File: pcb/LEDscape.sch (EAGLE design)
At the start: 31 parts, among them IC1 MAX3041CUE, IC2 MAX3041CUE, IC3 MAX3041CUE, IC4 MAX3041CUE, IC5 MAX3041CUE, IC6 MAX3041CUE, IC7 MAX3041CUE, IC8 MAX3041CUE

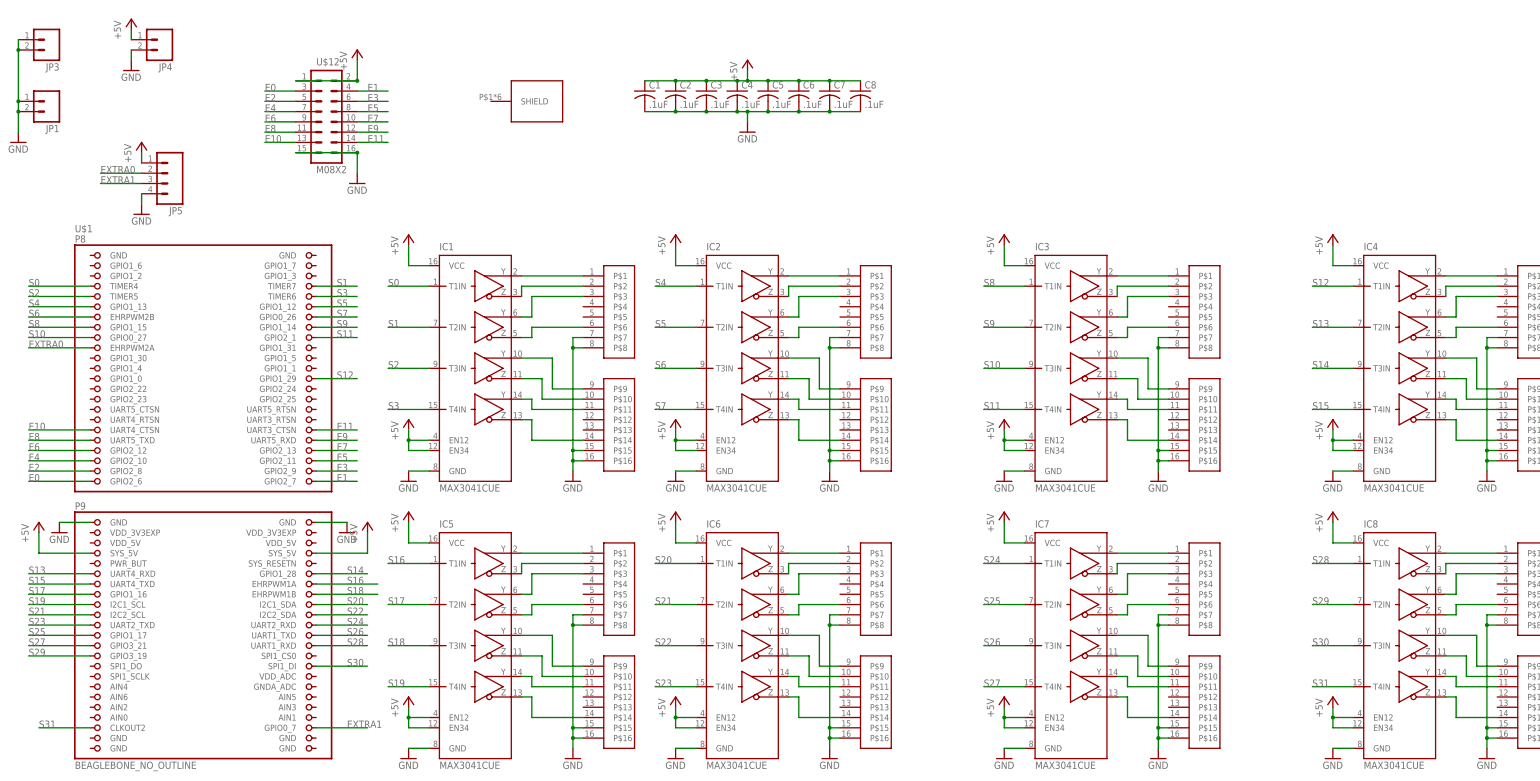
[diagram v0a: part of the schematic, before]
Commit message: RevB LEDscape board design: slightly bigger, debug headers for all signals
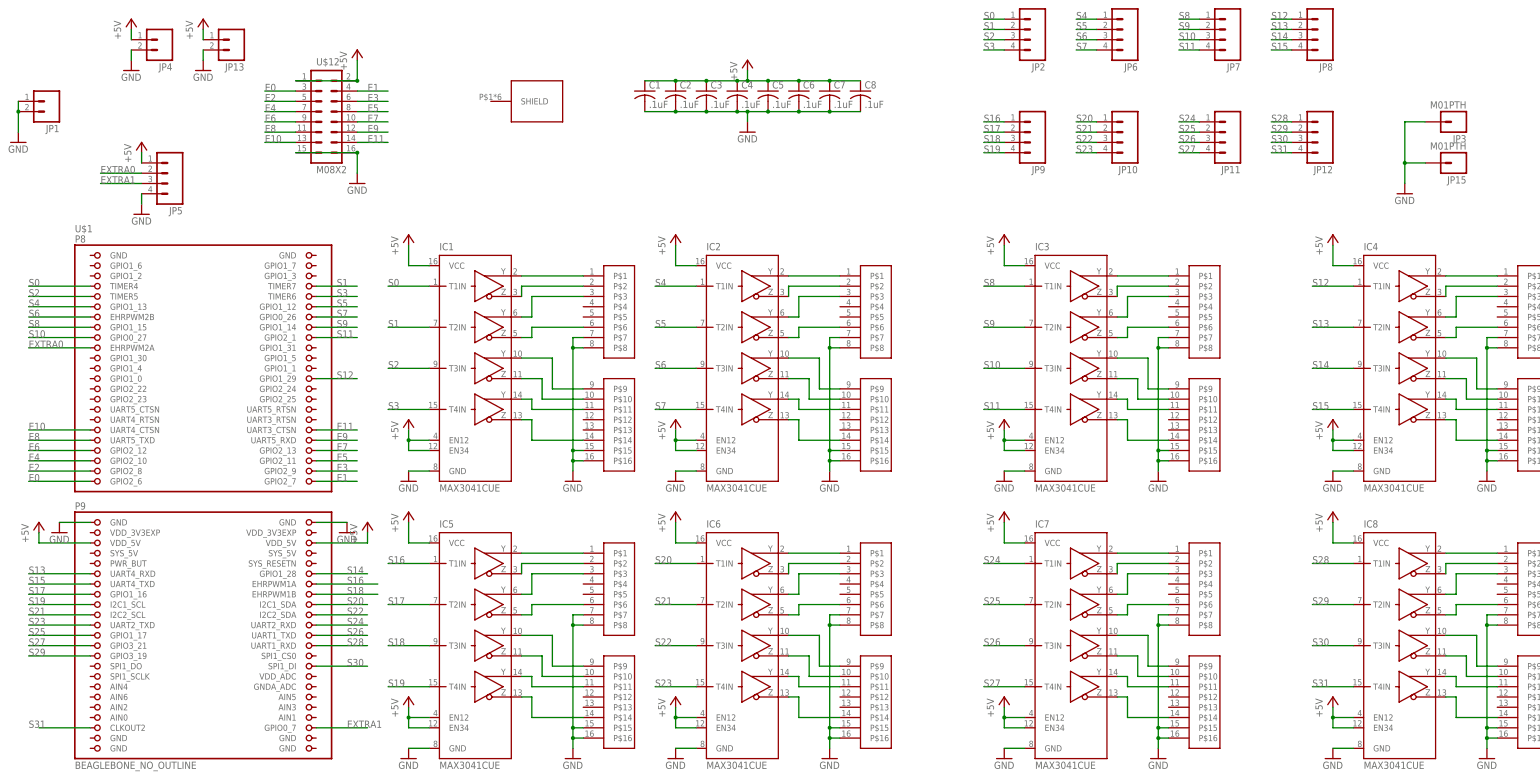
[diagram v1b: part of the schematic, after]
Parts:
- added JP10, JP11, JP12, JP2, JP6, JP7, JP8, JP9: (no value), SparkFun-Connectors:M041X04_NO_SILK
- added JP13: (no value), SparkFun-Connectors:M025MM
- added JP15: M01PTH, SparkFun-Connectors:M01PTH
- JP3: value (none) -> M01PTH; device SparkFun-Connectors:M025MM -> SparkFun-Connectors:M01PTH
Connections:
- net +5V: now also JP13.1, U$1.VDD_5V@1, U$1.VDD_5V@2; no longer U$1.SYS_5V@1, U$1.SYS_5V@2
- net GND: now also JP13.2, JP15.1; no longer JP3.2
- net S0: now also JP2.1
- net S1: now also JP2.2
- net S10: now also JP7.3
- net S11: now also JP7.4
- net S12: now also JP8.1
- net S13: now also JP8.2
- net S14: now also JP8.3
- net S15: now also JP8.4
- net S16: now also JP9.1
- net S17: now also JP9.2
- net S18: now also JP9.3
- net S19: now also JP9.4
- net S2: now also JP2.3
- net S20: now also JP10.1
- net S21: now also JP10.2
- net S22: now also JP10.3
- net S23: now also JP10.4
- net S24: now also JP11.1
- net S25: now also JP11.2
- net S26: now also JP11.3
- net S27: now also JP11.4
- net S28: now also JP12.1
- net S29: now also JP12.2
- net S3: now also JP2.4
- net S30: now also JP12.3
- net S31: now also JP12.4
- net S4: now also JP6.1
- net S5: now also JP6.2
- net S6: now also JP6.3
- net S7: now also JP6.4
- net S8: now also JP7.1
- net S9: now also JP7.2

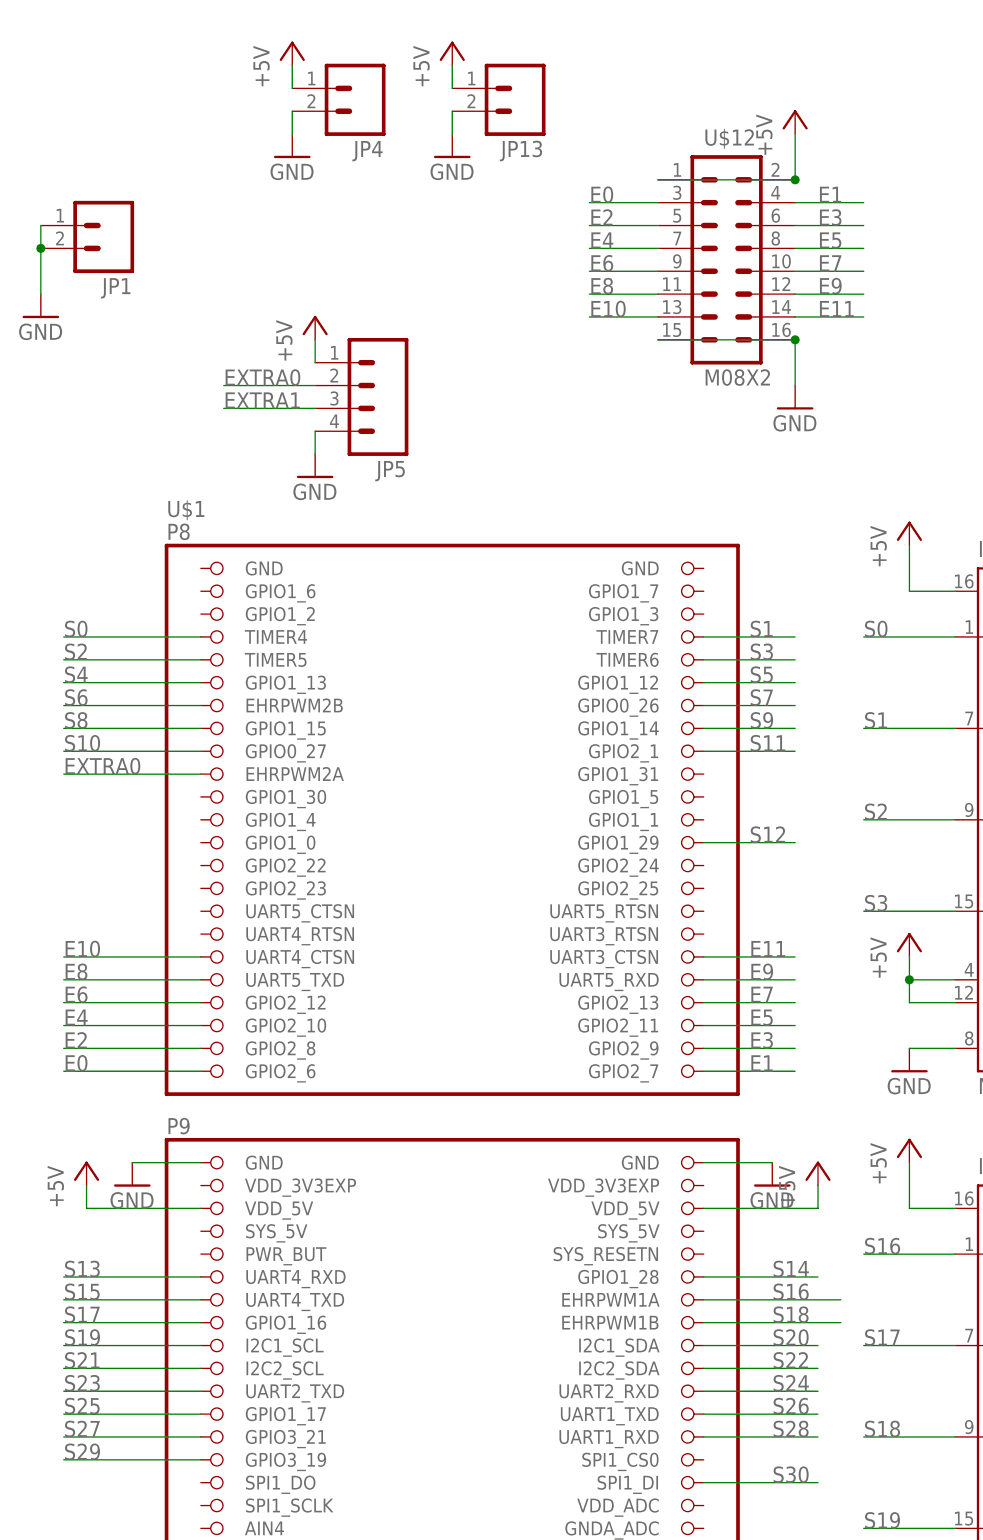
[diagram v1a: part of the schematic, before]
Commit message: Redesign transmitter PCB to use top and bottom ground planes, and one track for +5V- should be much easier to work with.
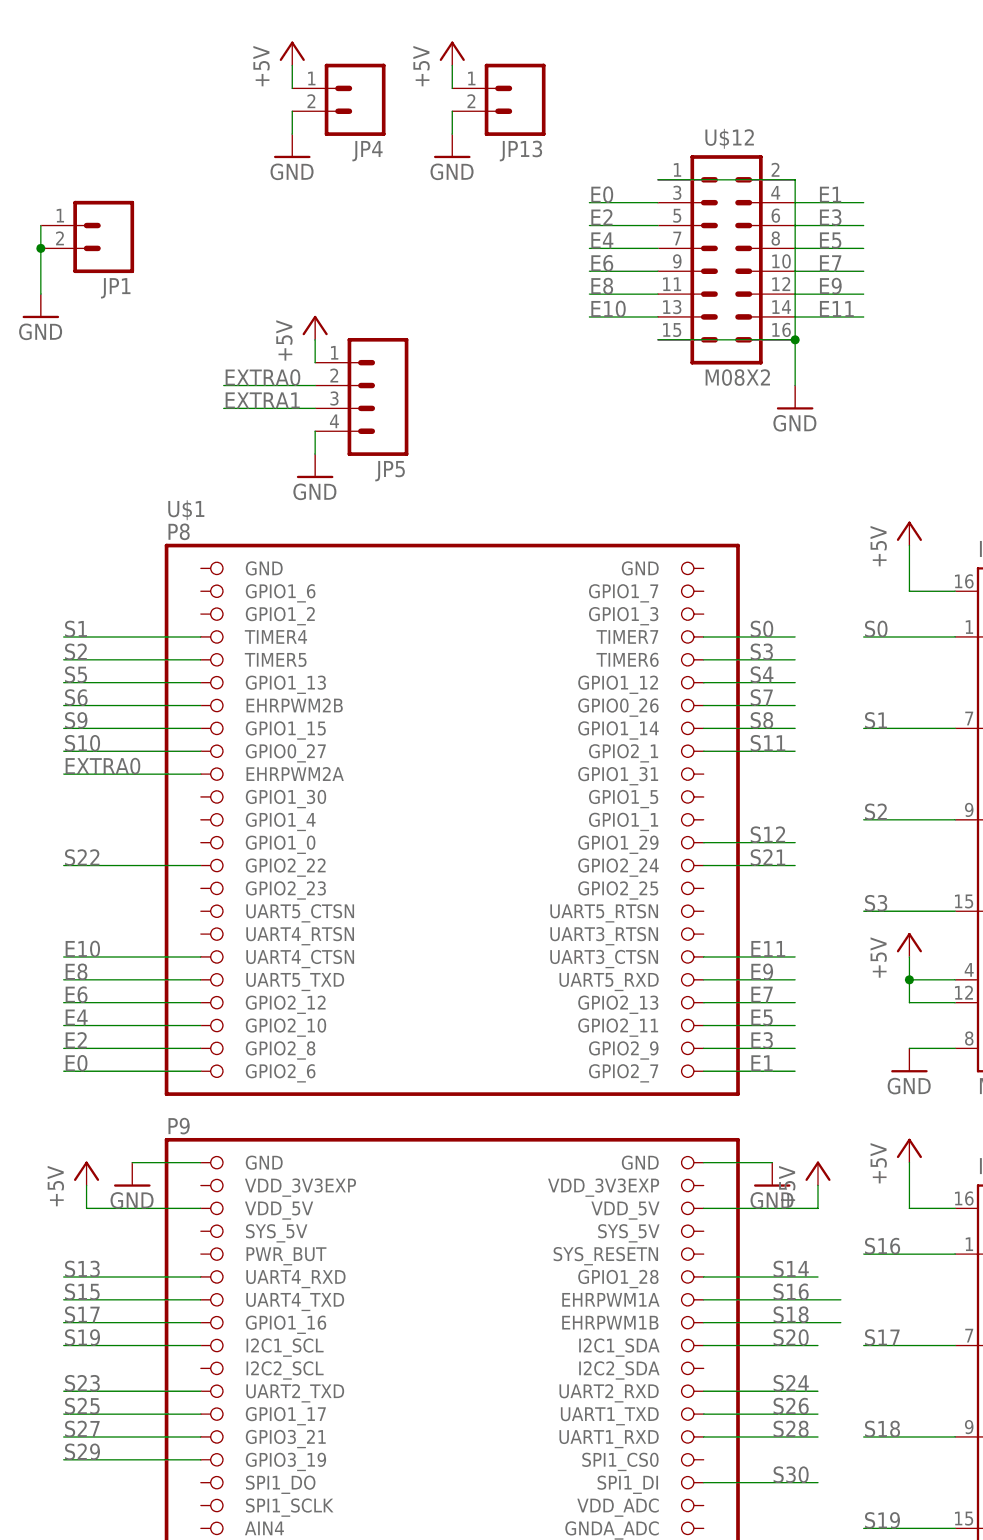
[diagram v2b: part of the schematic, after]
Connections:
- net +5V: no longer U$12.1, U$12.2
- net GND: now also U$12.1, U$12.2
- net S0: now also U$1.TIMER7; no longer U$1.TIMER4
- net S1: now also U$1.TIMER4; no longer U$1.TIMER7
- net S21: now also U$1.GPIO2_24; no longer U$1.I2C2_SCL
- net S22: now also U$1.GPIO2_22; no longer U$1.I2C2_SDA
- net S4: now also U$1.GPIO1_12; no longer U$1.GPIO1_13
- net S5: now also U$1.GPIO1_13; no longer U$1.GPIO1_12
- net S8: now also U$1.GPIO1_14; no longer U$1.GPIO1_15
- net S9: now also U$1.GPIO1_15; no longer U$1.GPIO1_14
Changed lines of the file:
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@@
 <part name="P+21" library="supply1" deviceset="+5V" device=""/>
 <part name="U$12" library="SparkFun-Connectors" deviceset="M08X2" device=""/>
-<part name="P+22" library="supply1" deviceset="+5V" device=""/>
 <part name="GND23" library="supply1" deviceset="GND" device=""/>
 <part name="JP5" library="SparkFun-Connectors" deviceset="M04" device="1X04_NO_SILK"/>
@@
 <instance part="P+21" gate="1" x="38.1" y="124.46"/>
 <instance part="U$12" gate="G$1" x="83.82" y="129.54"/>
-<instance part="P+22" gate="1" x="91.44" y="147.32"/>
 <instance part="GND23" gate="1" x="91.44" y="114.3"/>
 <instance part="JP5" gate="G$1" x="43.18" y="116.84" rot="R180"/>
@@
 </segment>
 <segment>
-<pinref part="U$12" gate="G$1" pin="1"/>
-<pinref part="U$12" gate="G$1" pin="2"/>
-<wire x1="76.2" y1="139.7" x2="91.44" y2="139.7" width="0.1524" layer="91"/>
-<wire x1="91.44" y1="144.78" x2="91.44" y2="139.7" width="0.1524" layer="91"/>
-<pinref part="P+22" gate="1" pin="+5V"/>
-<junction x="91.44" y="139.7"/>
-</segment>
-<segment>
 <pinref part="JP13" gate="G$1" pin="1"/>
 <wire x1="53.34" y1="149.86" x2="53.34" y2="152.4" width="0.1524" layer="91"/>
@@
 <pinref part="GND23" gate="1" pin="GND"/>
 <junction x="91.44" y="121.92"/>
+<pinref part="U$12" gate="G$1" pin="1"/>
+<pinref part="U$12" gate="G$1" pin="2"/>
+<wire x1="76.2" y1="139.7" x2="91.44" y2="139.7" width="0.1524" layer="91"/>
+<wire x1="91.44" y1="139.7" x2="91.44" y2="121.92" width="0.1524" layer="91"/>
 </segment>
 <segment>
@@
 </segment>
 <segment>
+<wire x1="251.46" y1="154.94" x2="246.38" y2="154.94" width="0.1524" layer="91"/>
+<label x="246.38" y="154.94" size="1.778" layer="95"/>
+<pinref part="JP2" gate="G$1" pin="1"/>
+</segment>
+<segment>
+<pinref part="U$1" gate="G$1" pin="TIMER7"/>
+<wire x1="81.28" y1="88.9" x2="91.44" y2="88.9" width="0.1524" layer="91"/>
+<label x="86.36" y="88.9" size="1.778" layer="95"/>
+</segment>
+</net>
+<net name="S1" class="0">
+<segment>
+<pinref part="IC1" gate="G$1" pin="T2IN"/>
+<wire x1="109.22" y1="78.74" x2="99.06" y2="78.74" width="0.1524" layer="91"/>
+<label x="99.06" y="78.74" size="1.778" layer="95"/>
+</segment>
+<segment>
+<wire x1="251.46" y1="152.4" x2="246.38" y2="152.4" width="0.1524" layer="91"/>
+<label x="246.38" y="152.4" size="1.778" layer="95"/>
+<pinref part="JP2" gate="G$1" pin="2"/>
+</segment>
+<segment>
 <pinref part="U$1" gate="G$1" pin="TIMER4"/>
 <wire x1="25.4" y1="88.9" x2="10.16" y2="88.9" width="0.1524" layer="91"/>
 <label x="10.16" y="88.9" size="1.778" layer="95"/>
 </segment>
-<segment>
-<wire x1="251.46" y1="154.94" x2="246.38" y2="154.94" width="0.1524" layer="91"/>
-<label x="246.38" y="154.94" size="1.778" layer="95"/>
-<pinref part="JP2" gate="G$1" pin="1"/>
-</segment>
-</net>
-<net name="S1" class="0">
-<segment>
-<pinref part="IC1" gate="G$1" pin="T2IN"/>
-<wire x1="109.22" y1="78.74" x2="99.06" y2="78.74" width="0.1524" layer="91"/>
-<label x="99.06" y="78.74" size="1.778" layer="95"/>
-</segment>
-<segment>
-<pinref part="U$1" gate="G$1" pin="TIMER7"/>
-<wire x1="81.28" y1="88.9" x2="91.44" y2="88.9" width="0.1524" layer="91"/>
-<label x="86.36" y="88.9" size="1.778" layer="95"/>
-</segment>
-<segment>
-<wire x1="251.46" y1="152.4" x2="246.38" y2="152.4" width="0.1524" layer="91"/>
-<label x="246.38" y="152.4" size="1.778" layer="95"/>
-<pinref part="JP2" gate="G$1" pin="2"/>
-</segment>
 </net>
 <net name="S2" class="0">
@@
 </segment>
 <segment>
+<wire x1="274.32" y1="154.94" x2="269.24" y2="154.94" width="0.1524" layer="91"/>
+<label x="269.24" y="154.94" size="1.778" layer="95"/>
+<pinref part="JP6" gate="G$1" pin="1"/>
+</segment>
+<segment>
+<pinref part="U$1" gate="G$1" pin="GPIO1_12"/>
+<wire x1="81.28" y1="83.82" x2="91.44" y2="83.82" width="0.1524" layer="91"/>
+<label x="86.36" y="83.82" size="1.778" layer="95"/>
+</segment>
+</net>
+<net name="S5" class="0">
+<segment>
+<pinref part="IC2" gate="G$1" pin="T2IN"/>
+<wire x1="175.26" y1="78.74" x2="165.1" y2="78.74" width="0.1524" layer="91"/>
+<label x="165.1" y="78.74" size="1.778" layer="95"/>
+</segment>
+<segment>
+<wire x1="269.24" y1="152.4" x2="274.32" y2="152.4" width="0.1524" layer="91"/>
+<label x="269.24" y="152.4" size="1.778" layer="95"/>
+<pinref part="JP6" gate="G$1" pin="2"/>
+</segment>
+<segment>
 <pinref part="U$1" gate="G$1" pin="GPIO1_13"/>
 <wire x1="25.4" y1="83.82" x2="10.16" y2="83.82" width="0.1524" layer="91"/>
 <label x="10.16" y="83.82" size="1.778" layer="95"/>
-</segment>
-<segment>
-<wire x1="274.32" y1="154.94" x2="269.24" y2="154.94" width="0.1524" layer="91"/>
-<label x="269.24" y="154.94" size="1.778" layer="95"/>
-<pinref part="JP6" gate="G$1" pin="1"/>
-</segment>
-</net>
-<net name="S5" class="0">
-<segment>
-<pinref part="IC2" gate="G$1" pin="T2IN"/>
-<wire x1="175.26" y1="78.74" x2="165.1" y2="78.74" width="0.1524" layer="91"/>
-<label x="165.1" y="78.74" size="1.778" layer="95"/>
-</segment>
-<segment>
-<pinref part="U$1" gate="G$1" pin="GPIO1_12"/>
-<wire x1="81.28" y1="83.82" x2="91.44" y2="83.82" width="0.1524" layer="91"/>
-<label x="86.36" y="83.82" size="1.778" layer="95"/>
-</segment>
-<segment>
-<wire x1="269.24" y1="152.4" x2="274.32" y2="152.4" width="0.1524" layer="91"/>
-<label x="269.24" y="152.4" size="1.778" layer="95"/>
-<pinref part="JP6" gate="G$1" pin="2"/>
 </segment>
 </net>
@@
 </segment>
 <segment>
+<wire x1="294.64" y1="154.94" x2="299.72" y2="154.94" width="0.1524" layer="91"/>
+<label x="294.64" y="154.94" size="1.778" layer="95"/>
+<pinref part="JP7" gate="G$1" pin="1"/>
+</segment>
+<segment>
+<pinref part="U$1" gate="G$1" pin="GPIO1_14"/>
+<wire x1="81.28" y1="78.74" x2="91.44" y2="78.74" width="0.1524" layer="91"/>
+<label x="86.36" y="78.74" size="1.778" layer="95"/>
+</segment>
+</net>
+<net name="S9" class="0">
+<segment>
+<pinref part="IC3" gate="G$1" pin="T2IN"/>
+<wire x1="256.54" y1="78.74" x2="246.38" y2="78.74" width="0.1524" layer="91"/>
+<label x="246.38" y="78.74" size="1.778" layer="95"/>
+</segment>
+<segment>
+<wire x1="299.72" y1="152.4" x2="294.64" y2="152.4" width="0.1524" layer="91"/>
+<label x="294.64" y="152.4" size="1.778" layer="95"/>
+<pinref part="JP7" gate="G$1" pin="2"/>
+</segment>
+<segment>
 <pinref part="U$1" gate="G$1" pin="GPIO1_15"/>
 <wire x1="25.4" y1="78.74" x2="10.16" y2="78.74" width="0.1524" layer="91"/>
 <label x="10.16" y="78.74" size="1.778" layer="95"/>
 </segment>
-<segment>
-<wire x1="294.64" y1="154.94" x2="299.72" y2="154.94" width="0.1524" layer="91"/>
-<label x="294.64" y="154.94" size="1.778" layer="95"/>
-<pinref part="JP7" gate="G$1" pin="1"/>
-</segment>
-</net>
-<net name="S9" class="0">
-<segment>
-<pinref part="IC3" gate="G$1" pin="T2IN"/>
-<wire x1="256.54" y1="78.74" x2="246.38" y2="78.74" width="0.1524" layer="91"/>
-<label x="246.38" y="78.74" size="1.778" layer="95"/>
-</segment>
-<segment>
-<pinref part="U$1" gate="G$1" pin="GPIO1_14"/>
-<wire x1="81.28" y1="78.74" x2="91.44" y2="78.74" width="0.1524" layer="91"/>
-<label x="86.36" y="78.74" size="1.778" layer="95"/>
-</segment>
-<segment>
-<wire x1="299.72" y1="152.4" x2="294.64" y2="152.4" width="0.1524" layer="91"/>
-<label x="294.64" y="152.4" size="1.778" layer="95"/>
-<pinref part="JP7" gate="G$1" pin="2"/>
-</segment>
 </net>
 <net name="S10" class="0">
@@
 </segment>
 <segment>
-<pinref part="U$1" gate="G$1" pin="I2C2_SCL"/>
-<wire x1="25.4" y1="7.62" x2="10.16" y2="7.62" width="0.1524" layer="91"/>
-<label x="10.16" y="7.62" size="1.778" layer="95"/>
-</segment>
-<segment>
 <wire x1="269.24" y1="127" x2="274.32" y2="127" width="0.1524" layer="91"/>
 <label x="269.24" y="127" size="1.778" layer="95"/>
 <pinref part="JP10" gate="G$1" pin="2"/>
 </segment>
+<segment>
+<pinref part="U$1" gate="G$1" pin="GPIO2_24"/>
+<wire x1="81.28" y1="63.5" x2="91.44" y2="63.5" width="0.1524" layer="91"/>
+<label x="86.36" y="63.5" size="1.778" layer="95"/>
+</segment>
 </net>
 <net name="S22" class="0">
@@
 </segment>
 <segment>
-<pinref part="U$1" gate="G$1" pin="I2C2_SDA"/>
-<wire x1="81.28" y1="7.62" x2="93.98" y2="7.62" width="0.1524" layer="91"/>
-<label x="88.9" y="7.62" size="1.778" layer="95"/>
-</segment>
-<segment>
 <wire x1="274.32" y1="124.46" x2="269.24" y2="124.46" width="0.1524" layer="91"/>
 <label x="269.24" y="124.46" size="1.778" layer="95"/>
 <pinref part="JP10" gate="G$1" pin="3"/>
 </segment>
-</net>
+<segment>
+<pinref part="U$1" gate="G$1" pin="GPIO2_22"/>
+<wire x1="25.4" y1="63.5" x2="10.16" y2="63.5" width="0.1524" layer="91"/>
+<label x="10.16" y="63.5" size="1.778" layer="95"/>
+</segment>
+</net>
